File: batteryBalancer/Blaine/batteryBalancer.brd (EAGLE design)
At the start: 101.6 x 101.6 mm, 32 parts

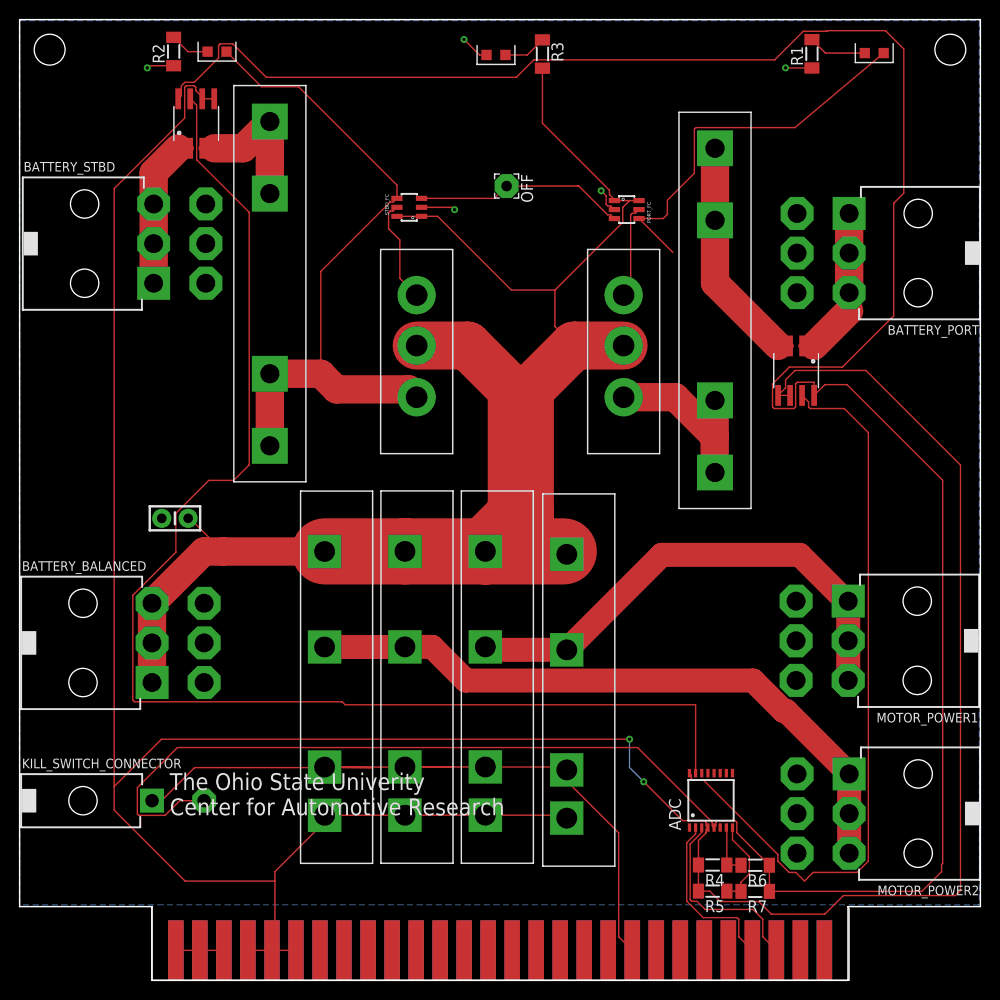
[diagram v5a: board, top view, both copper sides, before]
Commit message: Prettied up the routing and added kill switch indicator
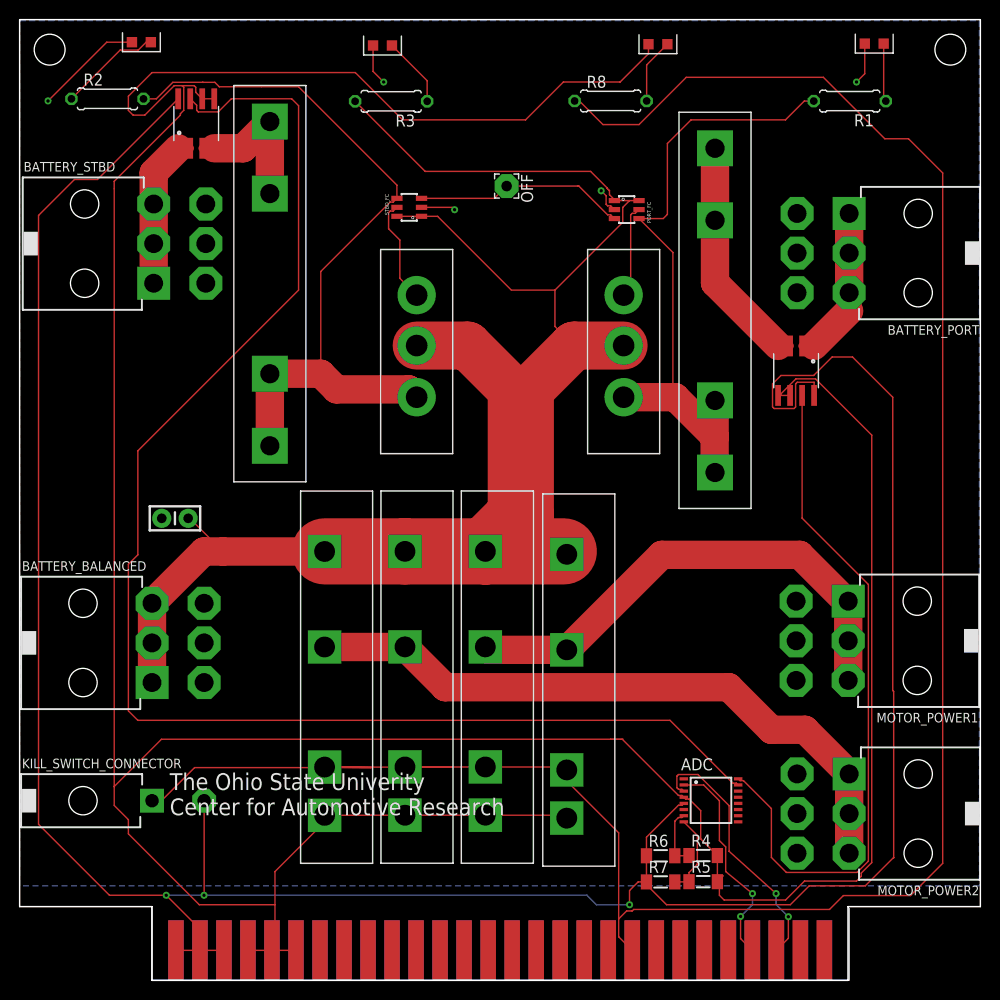
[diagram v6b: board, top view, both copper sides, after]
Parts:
- added KILL_STATUS: LTST-S270GKT, LTST-S270GKT:LTST-S270GKT
- added R8: 700, rcl:0207/7
- R1, R2, R3: device rcl:MINI_MELF-0204W -> rcl:0207/7
- moved R3 16.8 mm to (39.3, 93.0), turned to 180 degrees
- moved BALANCED_STATUS 12.0 mm to (38.4, 98.9)
- moved R6 10.0 mm to (67.8, 13.2), turned to 0 degrees
- moved R7 10.0 mm to (67.8, 10.4), turned to 0 degrees
- moved R2 8.60 mm to (9.29, 93.2), turned to 0 degrees
- moved STBD_STATUS 8.06 mm to (12.9, 99.2)
- moved R1 6.40 mm to (87.8, 93.0), turned to 180 degrees
- moved R4 1.41 mm to (72.3, 13.2), turned to 0 degrees
- moved R5 1.41 mm to (72.3, 10.4), turned to 0 degrees
- moved PORT_STATUS 1.00 mm to (90.4, 99.1)
- turned ADC to 0 degrees
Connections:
- removed net PORT_INDICATOR: PORT_STATUS.CATHODE, R1.2
- removed net STBD_INDICATOR: R2.2, STBD_STATUS.CATHODE
- new net N$3: KILL_STATUS.ANODE, R8.2
- new net PORT_STATUS: PORT_STATUS.ANODE, R1.1
- new net STBD_STATUS: R2.1, STBD_STATUS.ANODE
- net GND: now also PORT_STATUS.CATHODE, STBD_STATUS.CATHODE; no longer R1.1, R2.1
- net KILL_SWITCH: now also R8.1
- net LOGIC_GND: now also KILL_STATUS.CATHODE
- net N$1: now also R1.2; no longer PORT_STATUS.ANODE
- net STBD_UNBALANCED: now also R2.2; no longer STBD_STATUS.ANODE
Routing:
- net KILL_SWITCH: track 87.3 -> 243.2 mm
- net LOGIC_GND: track 330.2 -> 380.7 mm, vias 2 -> 0
- net 3.3V: track 312.8 -> 291.3 mm, vias 0 -> 3
- net BALANCED_POWER: track 163.6 -> 178.6 mm
- net STBD_CURRENT: track 139.8 -> 152.4 mm
- net GND: track 15.1 -> 26.6 mm
- net STBD_STATUS: track 0.00 -> 10.9 mm
- net STBD_UNBALANCED: track 71.5 -> 79.7 mm
- net SCL: track 20.6 -> 27.7 mm, vias 0 -> 2
- net N$1: track 60.4 -> 67.5 mm
- net N$3: track 0.00 -> 6.91 mm
- net PORT_INDICATOR: track 6.18 -> 0.00 mm
- net PORT_CURRENT: track 79.4 -> 73.5 mm
- net PORT_STATUS: track 0.00 -> 5.85 mm
- net SDA: track 18.3 -> 22.9 mm, vias 0 -> 2
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
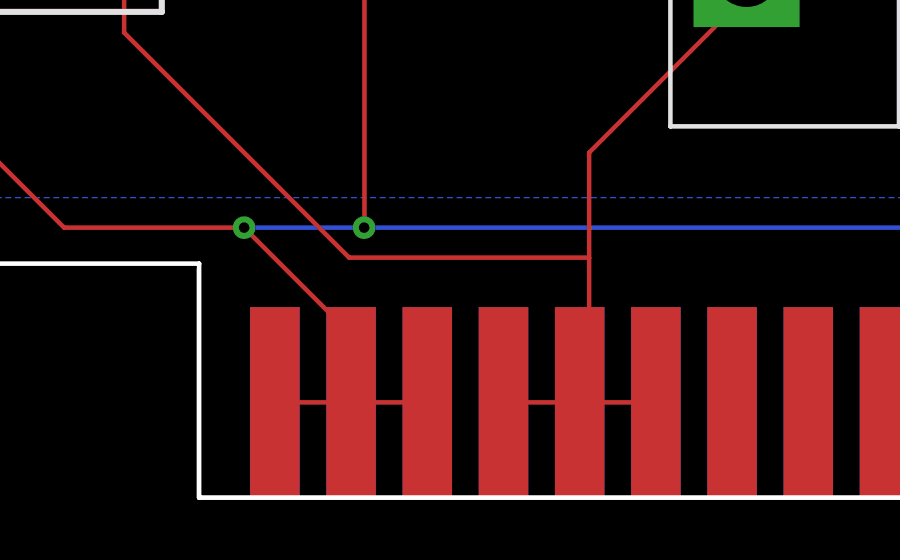
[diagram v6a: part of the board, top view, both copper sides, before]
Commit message: Lost all my work :( but at least I got the new edge connector
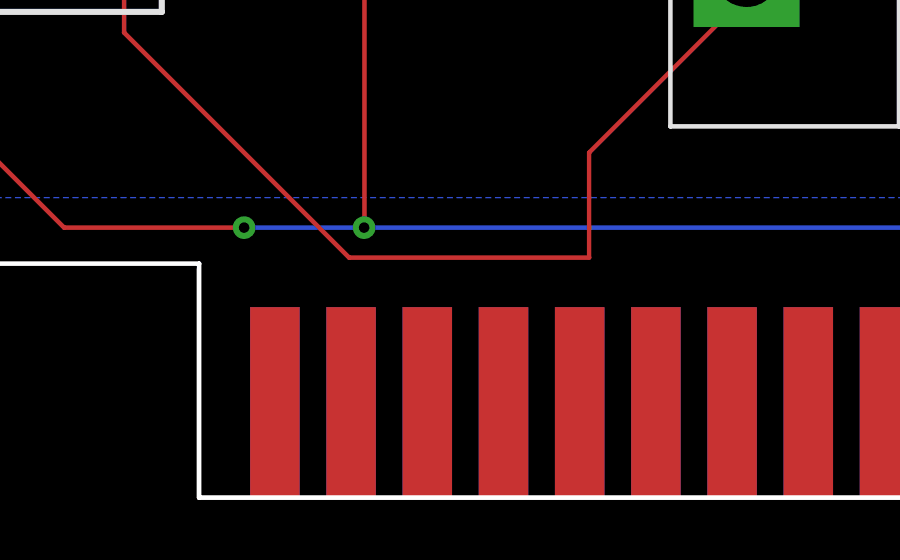
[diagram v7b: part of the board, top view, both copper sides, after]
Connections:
- net 3.3V: now also EDGE_CONNECTOR.3.3V_4, EDGE_CONNECTOR.3.3V_5, EDGE_CONNECTOR.3.3V_6
- net LOGIC_GND: now also EDGE_CONNECTOR.GND_4, EDGE_CONNECTOR.GND_5, EDGE_CONNECTOR.GND_6
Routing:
- net 3.3V: track 291.3 -> 278.9 mm
- net LOGIC_GND: track 380.7 -> 371.5 mm
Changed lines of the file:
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@@
 <wire x1="40.75" y1="17.4675" x2="37.2625" y2="17.4675" width="0.1524" layer="1"/>
 <wire x1="37.2625" y1="17.4675" x2="32.25" y2="17.455" width="0.1524" layer="1"/>
-<wire x1="29.2255" y1="3.175" x2="26.6855" y2="3.175" width="0.1524" layer="1"/>
+<wire x1="29.2255" y1="3.175" x2="26.6855" y2="3.175" width="0" layer="19" extent="1-16"/>
 <wire x1="26.5" y1="3.175" x2="26.6855" y2="3.175" width="0.1524" layer="1"/>
-<wire x1="26.5" y1="3.175" x2="24.1455" y2="3.175" width="0.1524" layer="1"/>
+<wire x1="26.5" y1="3.175" x2="24.1455" y2="3.175" width="0" layer="19" extent="1-16"/>
 <wire x1="49.25" y1="17.4675" x2="57.55" y2="17.4675" width="0.15" layer="1"/>
 <wire x1="57.8625" y1="17.155" x2="57.55" y2="17.4675" width="0.15" layer="1"/>
@@
 <wire x1="32.25" y1="16.75" x2="27" y2="11.5" width="0.15" layer="1"/>
 <wire x1="27" y1="11.5" x2="27" y2="8" width="0.15" layer="1"/>
-<wire x1="27" y1="8" x2="27" y2="3.675" width="0.15" layer="1"/>
+<wire x1="27" y1="8" x2="27" y2="3.675" width="0" layer="19" extent="1-16"/>
 <wire x1="27" y1="3.675" x2="26.5" y2="3.175" width="0.15" layer="1"/>
 <wire x1="10" y1="18.5" x2="10" y2="20.5" width="0.15" layer="1"/>
@@
 <wire x1="17" y1="91.651325" x2="17.356" y2="92.007325" width="0.1524" layer="1"/>
 <wire x1="17.191275" y1="94.6148" x2="18.461275" y2="94.6148" width="0.1524" layer="1"/>
+<contactref element="EDGE_CONNECTOR" pad="GND_6"/>
+<contactref element="EDGE_CONNECTOR" pad="GND_4"/>
+<contactref element="EDGE_CONNECTOR" pad="GND_5"/>
+<wire x1="29.2255" y1="3.175" x2="29.2255" y2="3.175" width="0" layer="19" extent="1-16"/>
+<wire x1="26.6855" y1="3.175" x2="26.6855" y2="3.175" width="0" layer="19" extent="1-16"/>
+<wire x1="24.1455" y1="3.175" x2="24.1455" y2="3.175" width="0" layer="19" extent="1-16"/>
 </signal>
 <signal name="PORT_UNBALANCED">
@@
 <contactref element="R7" pad="1"/>
 <contactref element="KILL_SWITCH_CONNECTOR" pad="2"/>
-<wire x1="21.6055" y1="3.175" x2="19.0655" y2="3.175" width="0.1524" layer="1"/>
-<wire x1="19.0655" y1="3.175" x2="16.5255" y2="3.175" width="0.1524" layer="1"/>
+<wire x1="21.6055" y1="3.175" x2="19.0655" y2="3.175" width="0" layer="19" extent="1-16"/>
+<wire x1="19.0655" y1="3.175" x2="16.5255" y2="3.175" width="0" layer="19" extent="1-16"/>
 <wire x1="81.898775" y1="60.4727" x2="82.0635" y2="60.637425" width="0.1524" layer="1"/>
 <wire x1="82.0635" y1="60.637425" x2="82.0635" y2="63.080175" width="0.1524" layer="1"/>
@@
 <wire x1="19.5" y1="9" x2="15.5" y2="9" width="0.1524" layer="16"/>
 <via x="15.5" y="9" extent="1-16" drill="0.35"/>
-<wire x1="19.0655" y1="3.175" x2="19.0655" y2="5.4345" width="0.1524" layer="1"/>
-<wire x1="19.0655" y1="5.4345" x2="15.5" y2="9" width="0.1524" layer="1"/>
+<wire x1="19.0655" y1="3.175" x2="19.0655" y2="5.4345" width="0" layer="19" extent="1-16"/>
+<wire x1="19.0655" y1="5.4345" x2="15.5" y2="9" width="0" layer="19" extent="1-16"/>
 <wire x1="15.5" y1="9" x2="9.5" y2="9" width="0.1524" layer="1"/>
 <wire x1="9.5" y1="9" x2="2" y2="16.5" width="0.1524" layer="1"/>
+<contactref element="EDGE_CONNECTOR" pad="3.3V_6"/>
+<contactref element="EDGE_CONNECTOR" pad="3.3V_4"/>
+<contactref element="EDGE_CONNECTOR" pad="3.3V_5"/>
+<wire x1="21.6055" y1="3.175" x2="21.6055" y2="3.175" width="0" layer="19" extent="1-16"/>
+<wire x1="19.0655" y1="3.175" x2="19.0655" y2="3.175" width="0" layer="19" extent="1-16"/>
+<wire x1="16.5255" y1="3.175" x2="16.5255" y2="3.175" width="0" layer="19" extent="1-16"/>
 </signal>
 <signal name="ADC_A0">

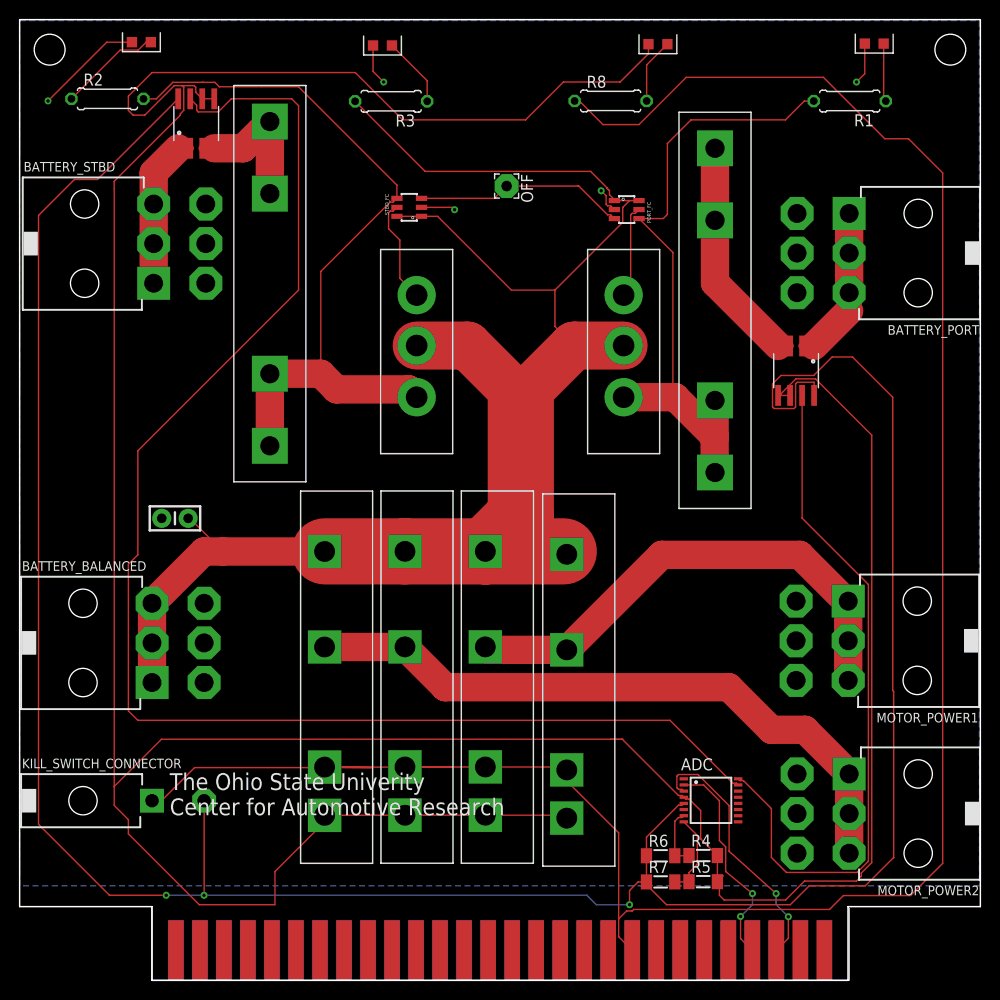
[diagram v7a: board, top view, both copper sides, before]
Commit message: Applied changes suggested in design review
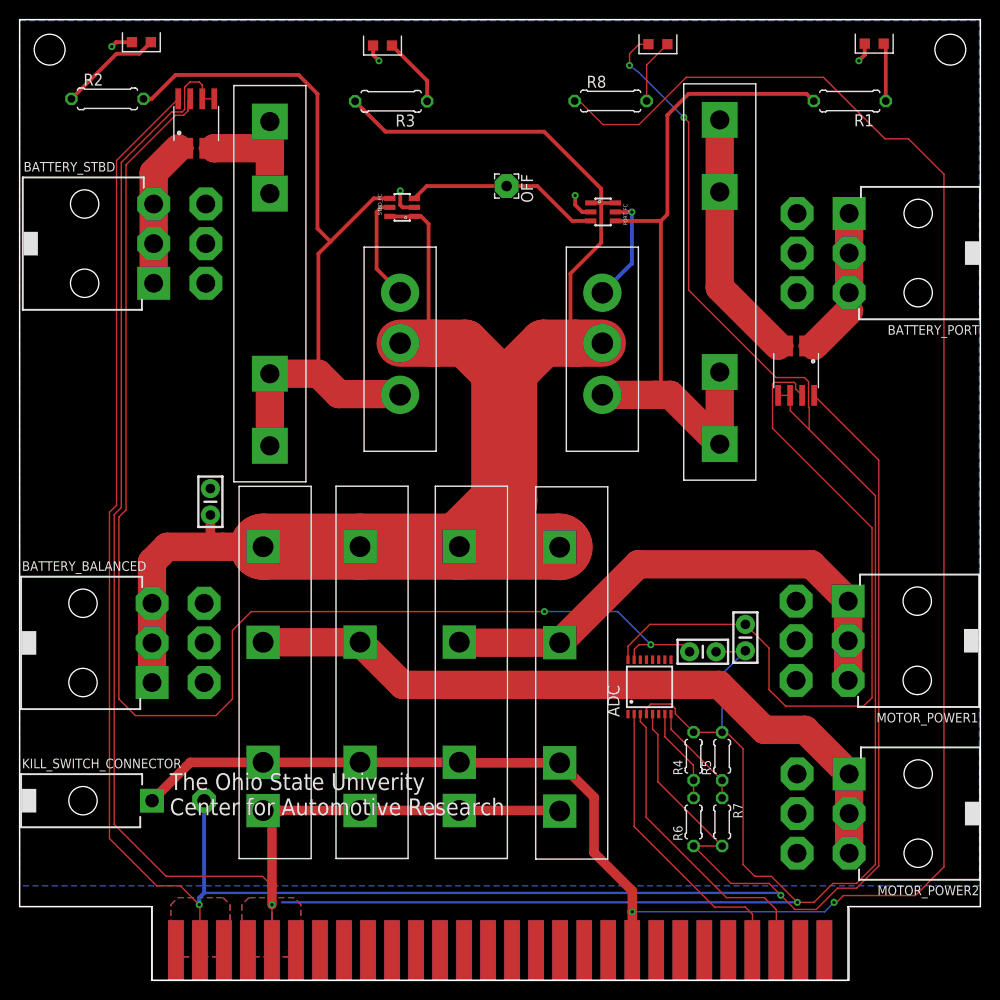
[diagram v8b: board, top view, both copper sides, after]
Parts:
- added C2, C3: 0.1uF, SparkFun-Capacitors:CAP-PTH-SMALL-KIT
- R4, R5, R6, R7: device rcl:MINI_MELF-0204W -> resistor:0204/5
- moved ADC 13.6 mm to (66.6, 31.0), turned to 90 degrees
- moved R5 13.4 mm to (74.3, 23.7), turned to 90 degrees
- moved R4 10.5 mm to (71.3, 23.7), turned to 90 degrees
- moved R7 9.08 mm to (74.3, 16.8), turned to 270 degrees
- moved RELAY4 6.52 mm to (25.8, 31.9)
- moved R6 4.99 mm to (71.3, 16.8), turned to 90 degrees
- moved RELAY3 4.78 mm to (36.0, 31.9)
- moved C1 4.14 mm to (20.2, 50.6), turned to 270 degrees
- moved PORT_FUSE 3.04 mm to (74.0, 74.5)
- moved RELAY2 2.80 mm to (46.5, 31.9)
- moved PORT_FC 2.51 mm to (61.7, 81.3)
- moved PORT_FET 2.26 mm to (61.6, 66.1)
- moved STBD_FET 1.77 mm to (40.2, 66.1)
- moved RLAY1 1.06 mm to (57.1, 31.9)
- moved STBD_FC 0.75 mm to (40.5, 81.8)
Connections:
- net N$1 renamed PORT_SOURCE
- net 3.3V: now also R7.2; no longer R7.1
- net ADC_A1: now also R7.1; no longer R7.2
- net LOGIC_GND: now also C2.2, C3.2
- net PORT_CURRENT: now also C3.1
- net STBD_CURRENT: now also C2.1
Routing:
- net KILL_SWITCH: track 243.2 -> 222.4 mm, vias 0 -> 2
- net GND: track 26.6 -> 12.3 mm
- net 3.3V: track 278.9 -> 267.7 mm, vias 3 -> 2
- net STBD_CURRENT: track 152.4 -> 141.8 mm, vias 0 -> 2
- net SDA: track 22.9 -> 32.1 mm, vias 2 -> 0
- net PORT_SOURCE: track 67.5 -> 75.3 mm
- net MOTOR_POWER2: track 69.4 -> 76.1 mm
- net SCL: track 27.7 -> 33.3 mm, vias 2 -> 0
- net ADC_A0: track 6.36 -> 10.1 mm
- net PORT_CURRENT: track 73.5 -> 76.3 mm
- net PORT_UNBALANCED: track 24.9 -> 27.7 mm
- net BALANCED_POWER: track 178.6 -> 176.0 mm
- net ADC_A1: track 8.79 -> 11.1 mm
- net LOGIC_GND: track 371.5 -> 373.3 mm, vias 0 -> 4
- net STBD_UNBALANCED: track 79.7 -> 81.5 mm
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- added copper zone on layer 1, net 3.3V
- added copper zone on layer 16, net 3.3V
- added copper zone on layer 1, net LOGIC_GND
- added copper zone on layer 16, net LOGIC_GND
